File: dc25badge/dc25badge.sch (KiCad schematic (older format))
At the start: 35 parts, among them P1 BATT, P2 USB_OTG, P3 CORTEX, Q1 DMN1019USN, SW1 RESET, SW3 MODE, SW4 BRIGHT, U1 MIC5305, U2 TPS61232, U3 ATSAMD21E18A-AU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

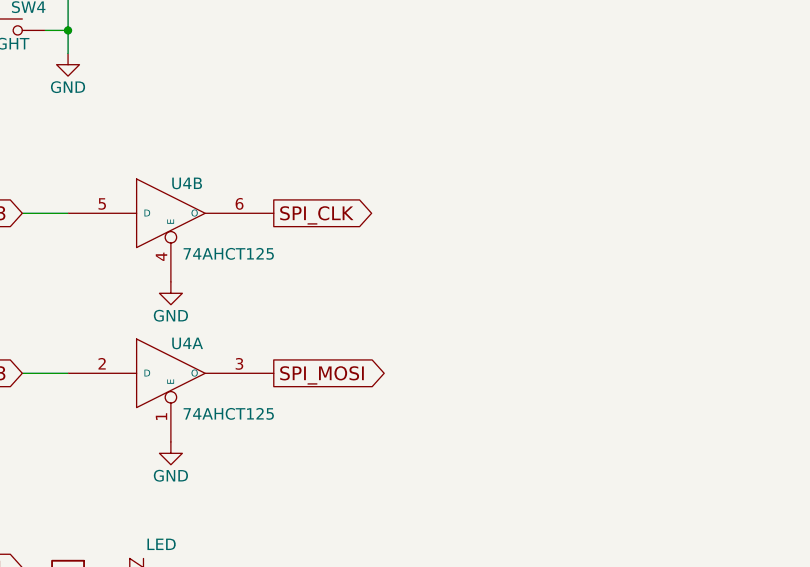
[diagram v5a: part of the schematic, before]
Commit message: Add option for anti-ringing resistors.
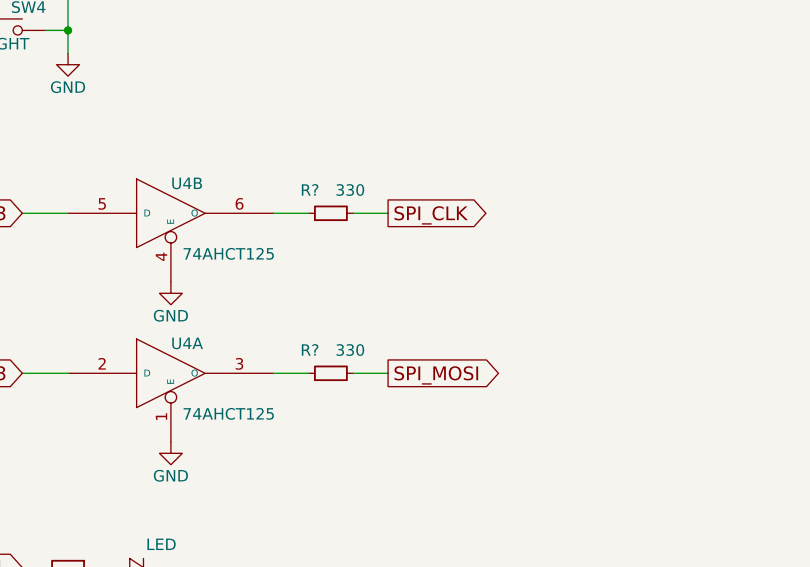
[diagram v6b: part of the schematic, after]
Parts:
- added R? (x2): 330, symbol R_Small
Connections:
- net SPI_CLK: now also R?.2; no longer U4.6 (O)
- net SPI_MOSI: now also R?.2; no longer U4.3 (O)
- new net: R?.1, U4.6 (O)
- new net: R?.1, U4.3 (O)
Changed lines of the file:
@@
 $EndDescr
 $Comp
-L +5V #PWR20
+L +5V #PWR01
 U 1 1 592A4C04
 P 5150 1950
-F 0 "#PWR20" H 5150 1800 50  0001 C CNN
+F 0 "#PWR01" H 5150 1800 50  0001 C CNN
 F 1 "+5V" H 5150 2090 50  0000 C CNN
 F 2 "" H 5150 1950 50  0000 C CNN
@@
 $EndComp
 $Comp
-L GND #PWR6
+L GND #PWR02
 U 1 1 592A5659
 P 1600 2550
-F 0 "#PWR6" H 1600 2300 50  0001 C CNN
+F 0 "#PWR02" H 1600 2300 50  0001 C CNN
 F 1 "GND" H 1600 2400 50  0000 C CNN
 F 2 "" H 1600 2550 50  0000 C CNN
@@
 $EndComp
 $Comp
-L GND #PWR7
+L GND #PWR03
 U 1 1 592A568F
 P 1650 1350
-F 0 "#PWR7" H 1650 1100 50  0001 C CNN
+F 0 "#PWR03" H 1650 1100 50  0001 C CNN
 F 1 "GND" H 1650 1200 50  0000 C CNN
 F 2 "" H 1650 1350 50  0000 C CNN
@@
 $EndComp
 $Comp
-L +3V3 #PWR12
+L +3V3 #PWR04
 U 1 1 592A5759
 P 2400 850
-F 0 "#PWR12" H 2400 700 50  0001 C CNN
+F 0 "#PWR04" H 2400 700 50  0001 C CNN
 F 1 "+3V3" H 2400 990 50  0000 C CNN
 F 2 "" H 2400 850 50  0000 C CNN
@@
 $EndComp
 $Comp
-L GND #PWR10
+L GND #PWR05
 U 1 1 592A794C
 P 2200 5650
-F 0 "#PWR10" H 2200 5400 50  0001 C CNN
+F 0 "#PWR05" H 2200 5400 50  0001 C CNN
 F 1 "GND" H 2200 5500 50  0000 C CNN
 F 2 "" H 2200 5650 50  0000 C CNN
@@
 $EndComp
 $Comp
-L +3V3 #PWR4
+L +3V3 #PWR06
 U 1 1 592A7D9A
 P 1400 4900
-F 0 "#PWR4" H 1400 4750 50  0001 C CNN
+F 0 "#PWR06" H 1400 4750 50  0001 C CNN
 F 1 "+3V3" H 1400 5040 50  0000 C CNN
 F 2 "" H 1400 4900 50  0000 C CNN
@@
 $EndComp
 $Comp
-L GND #PWR5
+L GND #PWR07
 U 1 1 592A7E37
 P 1400 5800
-F 0 "#PWR5" H 1400 5550 50  0001 C CNN
+F 0 "#PWR07" H 1400 5550 50  0001 C CNN
 F 1 "GND" H 1400 5650 50  0000 C CNN
 F 2 "" H 1400 5800 50  0000 C CNN
@@
 $EndComp
 $Comp
-L GND #PWR16
+L GND #PWR08
 U 1 1 592A8194
 P 3750 5750
-F 0 "#PWR16" H 3750 5500 50  0001 C CNN
+F 0 "#PWR08" H 3750 5500 50  0001 C CNN
 F 1 "GND" H 3750 5600 50  0000 C CNN
 F 2 "" H 3750 5750 50  0000 C CNN
@@
 $EndComp
 $Comp
-L +3V3 #PWR18
+L +3V3 #PWR09
 U 1 1 592A8397
 P 4200 5100
-F 0 "#PWR18" H 4200 4950 50  0001 C CNN
+F 0 "#PWR09" H 4200 4950 50  0001 C CNN
 F 1 "+3V3" H 4200 5240 50  0000 C CNN
 F 2 "" H 4200 5100 50  0000 C CNN
@@
 ~RESET
 $Comp
-L +3V3 #PWR8
+L +3V3 #PWR010
 U 1 1 592A8A6B
 P 1650 6150
-F 0 "#PWR8" H 1650 6000 50  0001 C CNN
+F 0 "#PWR010" H 1650 6000 50  0001 C CNN
 F 1 "+3V3" H 1650 6290 50  0000 C CNN
 F 2 "" H 1650 6150 50  0000 C CNN
@@
 $EndComp
 $Comp
-L GND #PWR9
+L GND #PWR011
 U 1 1 592A9161
 P 1650 7000
-F 0 "#PWR9" H 1650 6750 50  0001 C CNN
+F 0 "#PWR011" H 1650 6750 50  0001 C CNN
 F 1 "GND" H 1650 6850 50  0000 C CNN
 F 2 "" H 1650 7000 50  0000 C CNN
@@
 NoConn ~ 3250 6800
 $Comp
-L GND #PWR14
+L GND #PWR012
 U 1 1 592A986B
 P 2550 6950
-F 0 "#PWR14" H 2550 6700 50  0001 C CNN
+F 0 "#PWR012" H 2550 6700 50  0001 C CNN
 F 1 "GND" H 2550 6800 50  0000 C CNN
 F 2 "" H 2550 6950 50  0000 C CNN
@@
 $EndComp
 $Comp
-L +3V3 #PWR13
+L +3V3 #PWR013
 U 1 1 592A99A6
 P 2550 6500
-F 0 "#PWR13" H 2550 6350 50  0001 C CNN
+F 0 "#PWR013" H 2550 6350 50  0001 C CNN
 F 1 "+3V3" H 2550 6640 50  0000 C CNN
 F 2 "" H 2550 6500 50  0000 C CNN
@@
 $EndComp
 $Comp
-L GND #PWR2
+L GND #PWR014
 U 1 1 592AA720
 P 1250 4250
-F 0 "#PWR2" H 1250 4000 50  0001 C CNN
+F 0 "#PWR014" H 1250 4000 50  0001 C CNN
 F 1 "GND" H 1250 4100 50  0000 C CNN
 F 2 "" H 1250 4250 50  0000 C CNN
@@
 	1    0    0    -1
 $EndComp
-Text GLabel 7200 4600 2    60   Output ~ 0
+Text GLabel 7700 4600 2    60   Output ~ 0
 SPI_CLK
-Text GLabel 7200 5300 2    60   Output ~ 0
+Text GLabel 7700 5300 2    60   Output ~ 0
 SPI_MOSI
 Wire Wire Line
@@
 $EndComp
 $Comp
-L PWR_FLAG #FLG1
+L PWR_FLAG #FLG015
 U 1 1 592AD95C
 P 1150 1750
-F 0 "#FLG1" H 1150 1845 50  0001 C CNN
+F 0 "#FLG015" H 1150 1845 50  0001 C CNN
 F 1 "PWR_FLAG" H 1150 1930 50  0000 C CNN
 F 2 "" H 1150 1750 50  0000 C CNN
@@
 	4700 6700 4700 6800
 $Comp
-L +5V #PWR21
+L +5V #PWR016
 U 1 1 592AE3BE
 P 5250 6750
-F 0 "#PWR21" H 5250 6600 50  0001 C CNN
+F 0 "#PWR016" H 5250 6600 50  0001 C CNN
 F 1 "+5V" H 5250 6890 50  0000 C CNN
 F 2 "" H 5250 6750 50  0000 C CNN
@@
 	4250 6400 4250 7200
 $Comp
-L GND #PWR19
+L GND #PWR017
 U 1 1 592AE5B3
 P 4250 7200
-F 0 "#PWR19" H 4250 6950 50  0001 C CNN
+F 0 "#PWR017" H 4250 6950 50  0001 C CNN
 F 1 "GND" H 4250 7050 50  0000 C CNN
 F 2 "" H 4250 7200 50  0000 C CNN
@@
 Connection ~ 2150 3250
 $Comp
-L GND #PWR11
+L GND #PWR018
 U 1 1 592B1083
 P 2350 3600
-F 0 "#PWR11" H 2350 3350 50  0001 C CNN
+F 0 "#PWR018" H 2350 3350 50  0001 C CNN
 F 1 "GND" H 2350 3450 50  0000 C CNN
 F 2 "" H 2350 3600 50  0000 C CNN
@@
 	5700 3550 5800 3550
 $Comp
-L GND #PWR22
+L GND #PWR019
 U 1 1 592BA362
 P 6300 3900
-F 0 "#PWR22" H 6300 3650 50  0001 C CNN
+F 0 "#PWR019" H 6300 3650 50  0001 C CNN
 F 1 "GND" H 6300 3750 50  0000 C CNN
 F 2 "" H 6300 3900 50  0000 C CNN
@@
 $EndComp
 $Comp
-L GND #PWR17
+L GND #PWR020
 U 1 1 592C536E
 P 4150 2600
-F 0 "#PWR17" H 4150 2350 50  0001 C CNN
+F 0 "#PWR020" H 4150 2350 50  0001 C CNN
 F 1 "GND" H 4150 2450 50  0000 C CNN
 F 2 "" H 4150 2600 50  0000 C CNN
@@
 NoConn ~ 3700 1950
 $Comp
-L +5V #PWR15
+L +5V #PWR021
 U 1 1 592C61C0
 P 3500 2050
-F 0 "#PWR15" H 3500 1900 50  0001 C CNN
+F 0 "#PWR021" H 3500 1900 50  0001 C CNN
 F 1 "+5V" H 3500 2190 50  0000 C CNN
 F 2 "" H 3500 2050 50  0000 C CNN
@@
 NoConn ~ 1050 3300
 $Comp
-L GND #PWR1
+L GND #PWR022
 U 1 1 592CB85E
 P 850 4400
-F 0 "#PWR1" H 850 4150 50  0001 C CNN
+F 0 "#PWR022" H 850 4150 50  0001 C CNN
 F 1 "GND" H 850 4250 50  0000 C CNN
 F 2 "" H 850 4400 50  0000 C CNN
@@
 $EndComp
 $Comp
-L GND #PWR23
+L GND #PWR023
 U 1 1 59345803
 P 6750 4900
-F 0 "#PWR23" H 6750 4650 50  0001 C CNN
+F 0 "#PWR023" H 6750 4650 50  0001 C CNN
 F 1 "GND" H 6750 4750 50  0000 C CNN
 F 2 "" H 6750 4900 50  0000 C CNN
@@
 $EndComp
 $Comp
-L GND #PWR24
+L GND #PWR024
 U 1 1 5934585D
 P 6750 5600
-F 0 "#PWR24" H 6750 5350 50  0001 C CNN
+F 0 "#PWR024" H 6750 5350 50  0001 C CNN
 F 1 "GND" H 6750 5450 50  0000 C CNN
 F 2 "" H 6750 5600 50  0000 C CNN
@@
 $EndComp
 $Comp
-L GND #PWR25
+L GND #PWR025
 U 1 1 59347BAA
 P 6850 6250
-F 0 "#PWR25" H 6850 6000 50  0001 C CNN
+F 0 "#PWR025" H 6850 6000 50  0001 C CNN
 F 1 "GND" H 6850 6100 50  0000 C CNN
 F 2 "" H 6850 6250 50  0000 C CNN
@@
 Wire Wire Line
 	5650 1950 5650 2200
+$Comp
+L R_Small R?
+U 1 1 593B7147
+P 7450 4600
+F 0 "R?" V 7550 4650 50  0000 L CNN
+F 1 "330" V 7550 4450 50  0000 L CNN
+F 2 "" H 7450 4600 50  0000 C CNN
+F 3 "" H 7450 4600 50  0000 C CNN
+	1    7450 4600
+	0    -1   -1   0
+$EndComp
+$Comp
+L R_Small R?
+U 1 1 593B71D5
+P 7450 5300
+F 0 "R?" V 7550 5350 50  0000 L CNN
+F 1 "330" V 7550 5150 50  0000 L CNN
+F 2 "" H 7450 5300 50  0000 C CNN
+F 3 "" H 7450 5300 50  0000 C CNN
+	1    7450 5300
+	0    -1   -1   0
+$EndComp
+Wire Wire Line
+	7700 4600 7550 4600
+Wire Wire Line
+	7350 4600 7200 4600
+Wire Wire Line
+	7200 5300 7350 5300
+Wire Wire Line
+	7550 5300 7700 5300
 $EndSCHEMATC
